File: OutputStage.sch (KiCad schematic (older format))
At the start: 6 parts, among them Q12 AO4468, Q13 AO4468, Q3 AO4468, Q5 AO4468, U5 LM5175PWPR

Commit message: Lots of changes for MFG: parts info
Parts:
- L2: SKU (none) -> MWSA0603S-2R2MT
- Q12, Q13, Q3, Q5: footprint (none) -> SmartBattery:SOIC-8_Alpha_Omega; SKU (none) -> AO4468
- U5: footprint IC_TPS61196PWPRQ1 -> SmartBattery:IC_TPS61196PWPRQ1; SKU (none) -> LM5175PWPR
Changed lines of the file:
@@
 F 0 "U5" H 3550 6220 50  0000 C CNN
 F 1 "LM5175PWPR" H 3550 6129 50  0000 C CNN
-F 2 "IC_TPS61196PWPRQ1" H 3550 4350 50  0001 L BNN
+F 2 "SmartBattery:IC_TPS61196PWPRQ1" H 3550 4350 50  0001 L BNN
 F 3 "" H 3550 4350 50  0001 L BNN
+F 4 "LM5175PWPR" H 3550 4350 50  0001 C CNN "SKU"
 	1    3550 4350
 	1    0    0    -1
@@
 F 0 "Q3" H 6106 2046 50  0000 L CNN
 F 1 "AO4468" H 6106 1955 50  0000 L CNN
-F 2 "" H 6100 2100 50  0001 C CNN
+F 2 "SmartBattery:SOIC-8_Alpha_Omega" H 6100 2100 50  0001 C CNN
 F 3 "~" H 5900 2000 50  0001 C CNN
+F 4 "AO4468" H 5900 2000 50  0001 C CNN "SKU"
 	1    5900 2000
 	1    0    0    -1
@@
 F 0 "Q12" H 7506 1996 50  0000 L CNN
 F 1 "AO4468" H 7506 1905 50  0000 L CNN
-F 2 "" H 7500 2050 50  0001 C CNN
+F 2 "SmartBattery:SOIC-8_Alpha_Omega" H 7500 2050 50  0001 C CNN
 F 3 "~" H 7300 1950 50  0001 C CNN
+F 4 "AO4468" H 7300 1950 50  0001 C CNN "SKU"
 	1    7300 1950
 	1    0    0    -1
@@
 F 0 "Q5" H 6106 2946 50  0000 L CNN
 F 1 "AO4468" H 6106 2855 50  0000 L CNN
-F 2 "" H 6100 3000 50  0001 C CNN
+F 2 "SmartBattery:SOIC-8_Alpha_Omega" H 6100 3000 50  0001 C CNN
 F 3 "~" H 5900 2900 50  0001 C CNN
+F 4 "AO4468" H 5900 2900 50  0001 C CNN "SKU"
 	1    5900 2900
 	1    0    0    -1
@@
 F 0 "Q13" H 7556 2996 50  0000 L CNN
 F 1 "AO4468" H 7556 2905 50  0000 L CNN
-F 2 "" H 7550 3050 50  0001 C CNN
+F 2 "SmartBattery:SOIC-8_Alpha_Omega" H 7550 3050 50  0001 C CNN
 F 3 "~" H 7350 2950 50  0001 C CNN
+F 4 "AO4468" H 7350 2950 50  0001 C CNN "SKU"
 	1    7350 2950
 	1    0    0    -1
@@
 F 2 "SmartBattery:MWSA0603" H 5900 3900 50  0001 C CNN
 F 3 "~" H 5900 3900 50  0001 C CNN
+F 4 "MWSA0603S-2R2MT" V 5900 3900 50  0001 C CNN "SKU"
 	1    5900 3900
 	0    1    1    0

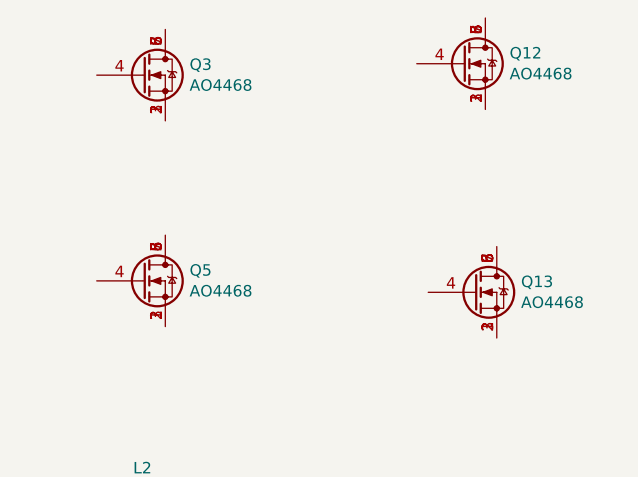
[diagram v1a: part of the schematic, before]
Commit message: Switching over to jlpcb
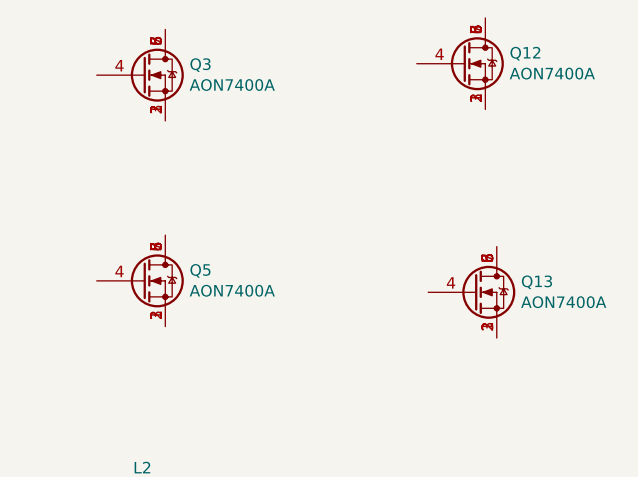
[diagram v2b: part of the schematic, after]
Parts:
- Q12, Q13, Q3, Q5: value AO4468 -> AON7400A; footprint SmartBattery:SOIC-8_Alpha_Omega -> lc_lib:QFN-8_3X3X065P; SKU AO4468 -> AON7400A
- U5: LCSC (none) -> C113356; SKU LM5175PWPR -> (none)
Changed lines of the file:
@@
 $Descr A4 11693 8268
 encoding utf-8
-Sheet 4 5
+Sheet 4 6
 Title ""
 Date ""
@@
 F 2 "SmartBattery:IC_TPS61196PWPRQ1" H 3550 4350 50  0001 L BNN
 F 3 "" H 3550 4350 50  0001 L BNN
-F 4 "LM5175PWPR" H 3550 4350 50  0001 C CNN "SKU"
+F 4 "C113356" H 3550 4350 50  0001 C CNN "LCSC"
 	1    3550 4350
 	1    0    0    -1
@@
 P 5900 2000
 F 0 "Q3" H 6106 2046 50  0000 L CNN
-F 1 "AO4468" H 6106 1955 50  0000 L CNN
-F 2 "SmartBattery:SOIC-8_Alpha_Omega" H 6100 2100 50  0001 C CNN
+F 1 "AON7400A " H 6106 1955 50  0000 L CNN
+F 2 "lc_lib:QFN-8_3X3X065P" H 6100 2100 50  0001 C CNN
 F 3 "~" H 5900 2000 50  0001 C CNN
-F 4 "AO4468" H 5900 2000 50  0001 C CNN "SKU"
+F 4 "AON7400A " H 5900 2000 50  0001 C CNN "SKU"
 	1    5900 2000
 	1    0    0    -1
@@
 P 7300 1950
 F 0 "Q12" H 7506 1996 50  0000 L CNN
-F 1 "AO4468" H 7506 1905 50  0000 L CNN
-F 2 "SmartBattery:SOIC-8_Alpha_Omega" H 7500 2050 50  0001 C CNN
+F 1 "AON7400A " H 7506 1905 50  0000 L CNN
+F 2 "lc_lib:QFN-8_3X3X065P" H 7500 2050 50  0001 C CNN
 F 3 "~" H 7300 1950 50  0001 C CNN
-F 4 "AO4468" H 7300 1950 50  0001 C CNN "SKU"
+F 4 "AON7400A " H 7300 1950 50  0001 C CNN "SKU"
 	1    7300 1950
 	1    0    0    -1
@@
 P 5900 2900
 F 0 "Q5" H 6106 2946 50  0000 L CNN
-F 1 "AO4468" H 6106 2855 50  0000 L CNN
-F 2 "SmartBattery:SOIC-8_Alpha_Omega" H 6100 3000 50  0001 C CNN
+F 1 "AON7400A " H 6106 2855 50  0000 L CNN
+F 2 "lc_lib:QFN-8_3X3X065P" H 6100 3000 50  0001 C CNN
 F 3 "~" H 5900 2900 50  0001 C CNN
-F 4 "AO4468" H 5900 2900 50  0001 C CNN "SKU"
+F 4 "AON7400A " H 5900 2900 50  0001 C CNN "SKU"
 	1    5900 2900
 	1    0    0    -1
@@
 P 7350 2950
 F 0 "Q13" H 7556 2996 50  0000 L CNN
-F 1 "AO4468" H 7556 2905 50  0000 L CNN
-F 2 "SmartBattery:SOIC-8_Alpha_Omega" H 7550 3050 50  0001 C CNN
+F 1 "AON7400A " H 7556 2905 50  0000 L CNN
+F 2 "lc_lib:QFN-8_3X3X065P" H 7550 3050 50  0001 C CNN
 F 3 "~" H 7350 2950 50  0001 C CNN
-F 4 "AO4468" H 7350 2950 50  0001 C CNN "SKU"
+F 4 "AON7400A " H 7350 2950 50  0001 C CNN "SKU"
 	1    7350 2950
 	1    0    0    -1

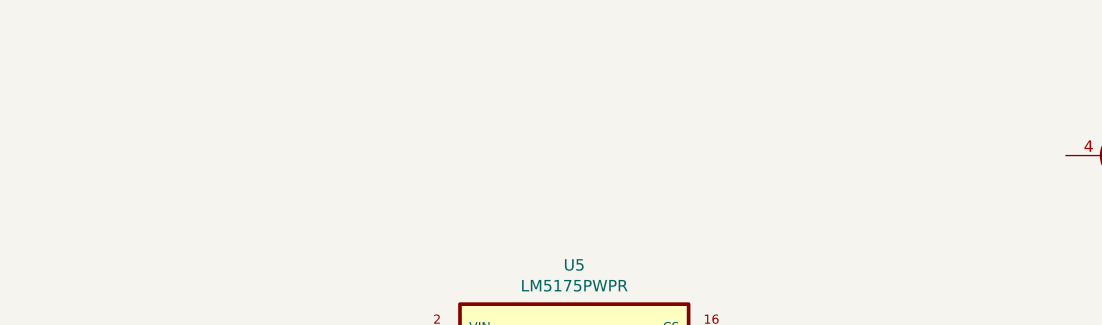
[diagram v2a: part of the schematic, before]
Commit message: Replaced old charger to support JLC assembly. Very close now!
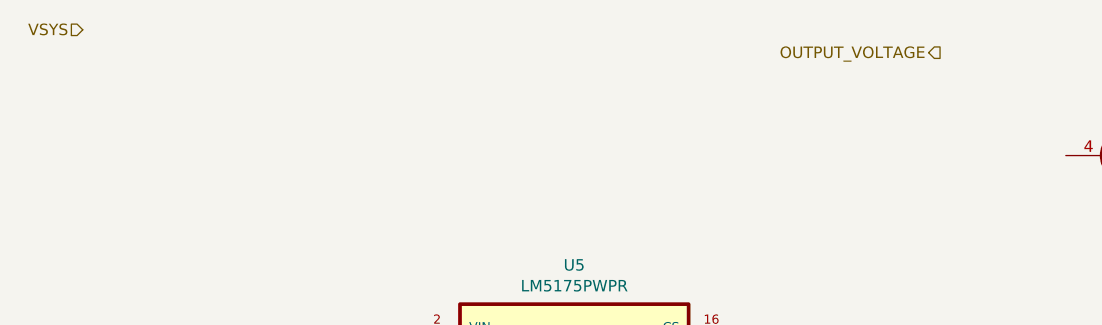
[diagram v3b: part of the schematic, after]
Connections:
- net labels added: OUTPUT_VOLTAGE, VSYS
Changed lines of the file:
@@
 Wire Wire Line
 	5200 3900 5750 3900
+Text HLabel 1400 1450 0    50   Input ~ 0
+VSYS
+Text HLabel 5150 1550 0    50   Output ~ 0
+OUTPUT_VOLTAGE
 $EndSCHEMATC

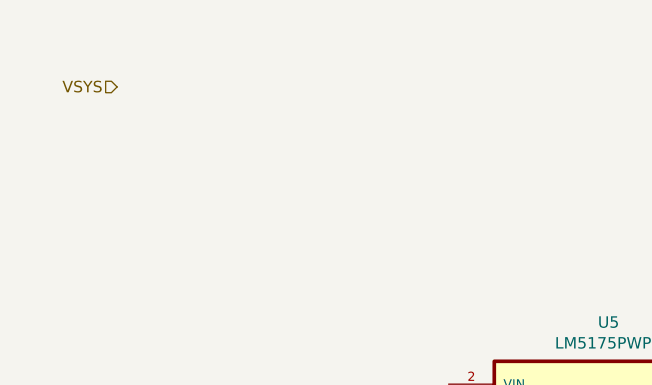
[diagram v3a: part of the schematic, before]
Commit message: Both type-c ports are done! Only outputstage left.
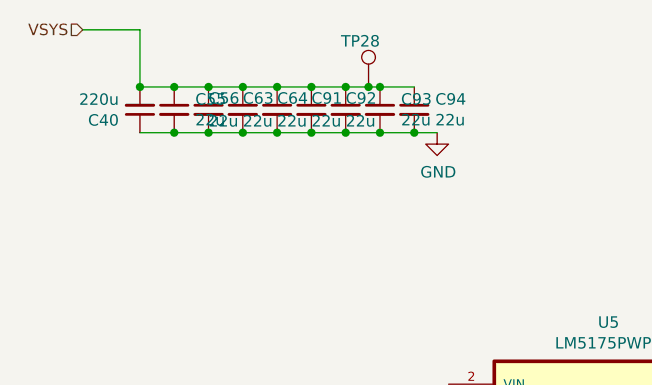
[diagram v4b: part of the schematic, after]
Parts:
- added C40: 220u, Capacitor_SMD:C_Elec_8x10.2, symbol Device:C_Small
- added C55, C56, C63, C64, C91, C92, C93, C94: 22u, lc_lib:0805_C, symbol Device:C_Small
- added TP28: TestPoint, TestPoint:TestPoint_Pad_D2.0mm, symbol Connector:TestPoint
- L2: footprint SmartBattery:MWSA0603 -> SmartBattery:L_10.3x11.5_H4
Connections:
- net labels added: GND
- wire segments 2 -> 22
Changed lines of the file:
@@
 $Descr A4 11693 8268
 encoding utf-8
-Sheet 4 6
+Sheet 4 8
 Title ""
 Date ""
@@
 F 0 "L2" V 5719 3900 50  0000 C CNN
 F 1 "MWSA0603-2R2MT" V 5810 3900 50  0000 C CNN
-F 2 "SmartBattery:MWSA0603" H 5900 3900 50  0001 C CNN
+F 2 "SmartBattery:L_10.3x11.5_H4" H 5900 3900 50  0001 C CNN
 F 3 "~" H 5900 3900 50  0001 C CNN
 F 4 "MWSA0603S-2R2MT" V 5900 3900 50  0001 C CNN "SKU"
@@
 Wire Wire Line
 	5200 3900 5750 3900
-Text HLabel 1400 1450 0    50   Input ~ 0
+Text HLabel 1250 1200 0    50   Input ~ 0
 VSYS
 Text HLabel 5150 1550 0    50   Output ~ 0
 OUTPUT_VOLTAGE
+$Comp
+L Device:C_Small C?
+U 1 1 5FF124CA
+P 1500 1550
+AR Path="/5FD99B08/5FF124CA" Ref="C?"  Part="1"
+AR Path="/60413DD6/5FF124CA" Ref="C40"  Part="1"
+F 0 "C40" H 1592 1596 50  0000 L CNN
+F 1 "220u" H 1592 1505 50  0000 L CNN
+F 2 "Capacitor_SMD:C_Elec_8x10.2" H 1500 1550 50  0001 C CNN
+F 3 "~" H 1500 1550 50  0001 C CNN
+F 4 "C311611" H 1500 1550 50  0001 C CNN "LCSC"
+	1    1500 1550
+	-1   0    0    1
+$EndComp
+$Comp
+L Connector:TestPoint TP?
+U 1 1 5FF124D0
+P 2500 1450
+AR Path="/5FD15753/5FF124D0" Ref="TP?"  Part="1"
+AR Path="/5FD99B08/5FF124D0" Ref="TP?"  Part="1"
+AR Path="/60413DD6/5FF124D0" Ref="TP28"  Part="1"
+F 0 "TP28" H 2550 1650 50  0000 R CNN
+F 1 "TestPoint" H 1950 1500 50  0001 R CNN
+F 2 "TestPoint:TestPoint_Pad_D2.0mm" H 2700 1450 50  0001 C CNN
+F 3 "~" H 2700 1450 50  0001 C CNN
+	1    2500 1450
+	1    0    0    -1
+$EndComp
+$Comp
+L Device:C_Small C?
+U 1 1 5FF12501
+P 2550 1550
+AR Path="/5FD99B08/5FF12501" Ref="C?"  Part="1"
+AR Path="/60413DD6/5FF12501" Ref="C93"  Part="1"
+F 0 "C93" H 2642 1596 50  0000 L CNN
+F 1 "22u" H 2642 1505 50  0000 L CNN
+F 2 "lc_lib:0805_C" H 2550 1550 50  0001 C CNN
+F 3 "~" H 2550 1550 50  0001 C CNN
+F 4 "C45783" H 2550 1550 50  0001 C CNN "LCSC"
+	1    2550 1550
+	1    0    0    -1
+$EndComp
+Connection ~ 2700 1650
+Wire Wire Line
+	2700 1650 2800 1650
+$Comp
+L power:GND #PWR0171
+U 1 1 5FF12523
+P 2800 1650
+F 0 "#PWR0171" H 2800 1400 50  0001 C CNN
+F 1 "GND" H 2805 1477 50  0000 C CNN
+F 2 "" H 2800 1650 50  0001 C CNN
+F 3 "" H 2800 1650 50  0001 C CNN
+	1    2800 1650
+	1    0    0    -1
+$EndComp
+Connection ~ 2500 1450
+Wire Wire Line
+	2500 1450 2550 1450
+Wire Wire Line
+	1500 1450 1650 1450
+Wire Wire Line
+	1800 1650 1950 1650
+$Comp
+L Device:C_Small C?
+U 1 1 5FF13851
+P 1800 1550
+AR Path="/5FD99B08/5FF13851" Ref="C?"  Part="1"
+AR Path="/60413DD6/5FF13851" Ref="C56"  Part="1"
+F 0 "C56" H 1800 1600 50  0000 L CNN
+F 1 "22u" H 1800 1500 50  0000 L CNN
+F 2 "lc_lib:0805_C" H 1800 1550 50  0001 C CNN
+F 3 "~" H 1800 1550 50  0001 C CNN
+F 4 "C45783" H 1800 1550 50  0001 C CNN "LCSC"
+	1    1800 1550
+	1    0    0    -1
+$EndComp
+Connection ~ 1800 1450
+Wire Wire Line
+	1800 1450 1950 1450
+$Comp
+L Device:C_Small C?
+U 1 1 5FF14635
+P 1950 1550
+AR Path="/5FD99B08/5FF14635" Ref="C?"  Part="1"
+AR Path="/60413DD6/5FF14635" Ref="C63"  Part="1"
+F 0 "C63" H 1950 1600 50  0000 L CNN
+F 1 "22u" H 1950 1500 50  0000 L CNN
+F 2 "lc_lib:0805_C" H 1950 1550 50  0001 C CNN
+F 3 "~" H 1950 1550 50  0001 C CNN
+F 4 "C45783" H 1950 1550 50  0001 C CNN "LCSC"
+	1    1950 1550
+	1    0    0    -1
+$EndComp
+Connection ~ 1950 1450
+Wire Wire Line
+	1950 1450 2100 1450
+Connection ~ 1950 1650
+Wire Wire Line
+	1950 1650 2100 1650
+$Comp
+L Device:C_Small C?
+U 1 1 5FF148DA
+P 2100 1550
+AR Path="/5FD99B08/5FF148DA" Ref="C?"  Part="1"
+AR Path="/60413DD6/5FF148DA" Ref="C64"  Part="1"
+F 0 "C64" H 2100 1600 50  0000 L CNN
+F 1 "22u" H 2100 1500 50  0000 L CNN
+F 2 "lc_lib:0805_C" H 2100 1550 50  0001 C CNN
+F 3 "~" H 2100 1550 50  0001 C CNN
+F 4 "C45783" H 2100 1550 50  0001 C CNN "LCSC"
+	1    2100 1550
+	1    0    0    -1
+$EndComp
+Connection ~ 2100 1450
+Wire Wire Line
+	2100 1450 2250 1450
+Connection ~ 2100 1650
+Wire Wire Line
+	2100 1650 2250 1650
+$Comp
+L Device:C_Small C?
+U 1 1 5FF14BE5
+P 2250 1550
+AR Path="/5FD99B08/5FF14BE5" Ref="C?"  Part="1"
+AR Path="/60413DD6/5FF14BE5" Ref="C91"  Part="1"
+F 0 "C91" H 2250 1600 50  0000 L CNN
+F 1 "22u" H 2250 1500 50  0000 L CNN
+F 2 "lc_lib:0805_C" H 2250 1550 50  0001 C CNN
+F 3 "~" H 2250 1550 50  0001 C CNN
+F 4 "C45783" H 2250 1550 50  0001 C CNN "LCSC"
+	1    2250 1550
+	1    0    0    -1
+$EndComp
+Connection ~ 2250 1450
+Wire Wire Line
+	2250 1450 2400 1450
+Connection ~ 2250 1650
+Wire Wire Line
+	2250 1650 2400 1650
+$Comp
+L Device:C_Small C?
+U 1 1 5FF14F44
+P 2400 1550
+AR Path="/5FD99B08/5FF14F44" Ref="C?"  Part="1"
+AR Path="/60413DD6/5FF14F44" Ref="C92"  Part="1"
+F 0 "C92" H 2400 1600 50  0000 L CNN
+F 1 "22u" H 2400 1500 50  0000 L CNN
+F 2 "lc_lib:0805_C" H 2400 1550 50  0001 C CNN
+F 3 "~" H 2400 1550 50  0001 C CNN
+F 4 "C45783" H 2400 1550 50  0001 C CNN "LCSC"
+	1    2400 1550
+	1    0    0    -1
+$EndComp
+Connection ~ 2400 1450
+Wire Wire Line
+	2400 1450 2500 1450
+Connection ~ 2400 1650
+Wire Wire Line
+	2400 1650 2550 1650
+Connection ~ 2550 1450
+Wire Wire Line
+	2550 1450 2700 1450
+Connection ~ 2550 1650
+Wire Wire Line
+	2550 1650 2700 1650
+$Comp
+L Device:C_Small C?
+U 1 1 5FF15579
+P 2700 1550
+AR Path="/5FD99B08/5FF15579" Ref="C?"  Part="1"
+AR Path="/60413DD6/5FF15579" Ref="C94"  Part="1"
+F 0 "C94" H 2792 1596 50  0000 L CNN
+F 1 "22u" H 2792 1505 50  0000 L CNN
+F 2 "lc_lib:0805_C" H 2700 1550 50  0001 C CNN
+F 3 "~" H 2700 1550 50  0001 C CNN
+F 4 "C45783" H 2700 1550 50  0001 C CNN "LCSC"
+	1    2700 1550
+	1    0    0    -1
+$EndComp
+$Comp
+L Device:C_Small C?
+U 1 1 5FF1591C
+P 1650 1550
+AR Path="/5FD99B08/5FF1591C" Ref="C?"  Part="1"
+AR Path="/60413DD6/5FF1591C" Ref="C55"  Part="1"
+F 0 "C55" H 1742 1596 50  0000 L CNN
+F 1 "22u" H 1742 1505 50  0000 L CNN
+F 2 "lc_lib:0805_C" H 1650 1550 50  0001 C CNN
+F 3 "~" H 1650 1550 50  0001 C CNN
+F 4 "C45783" H 1650 1550 50  0001 C CNN "LCSC"
+	1    1650 1550
+	1    0    0    -1
+$EndComp
+Connection ~ 1650 1450
+Wire Wire Line
+	1650 1450 1800 1450
+Wire Wire Line
+	1800 1650 1650 1650
+Connection ~ 1800 1650
+Wire Wire Line
+	1650 1650 1500 1650
+Connection ~ 1650 1650
+Wire Wire Line
+	1250 1200 1500 1200
+Wire Wire Line
+	1500 1200 1500 1450
+Connection ~ 1500 1450
 $EndSCHEMATC

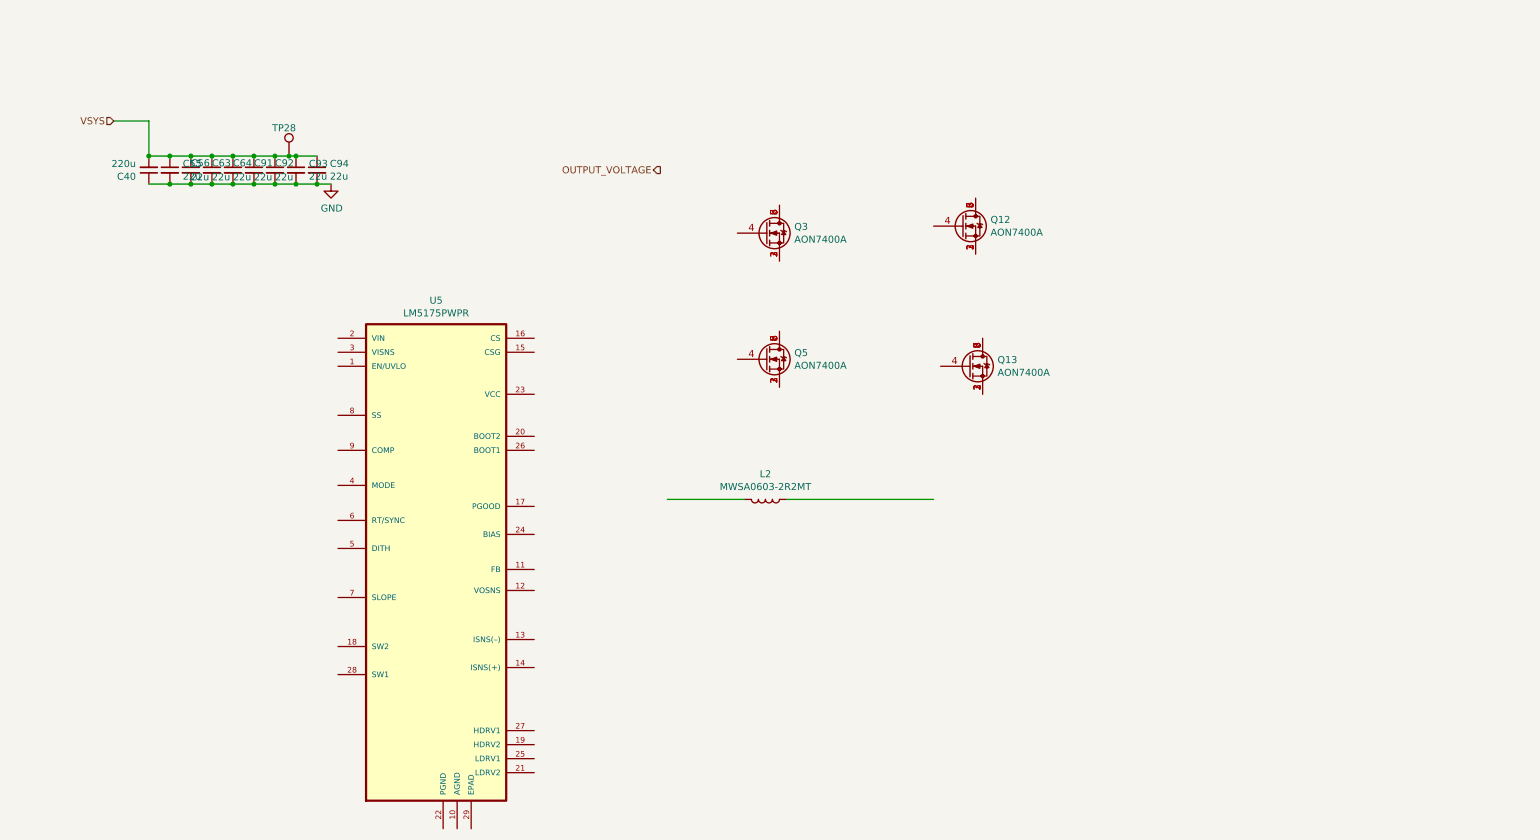
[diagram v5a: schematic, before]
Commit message: Type_A_implemented. Sch "locked". PCB Layout started.
*Changelog:
*Type-a switching regulator (TBD -- need to check inductor,caps, stability. Maybe check both peripherial inductors?)
*Type-A load switch + connector + esd
*started layout..
*found out that my footprint for n fet is wrong. Fixing now, need to replace all of those.
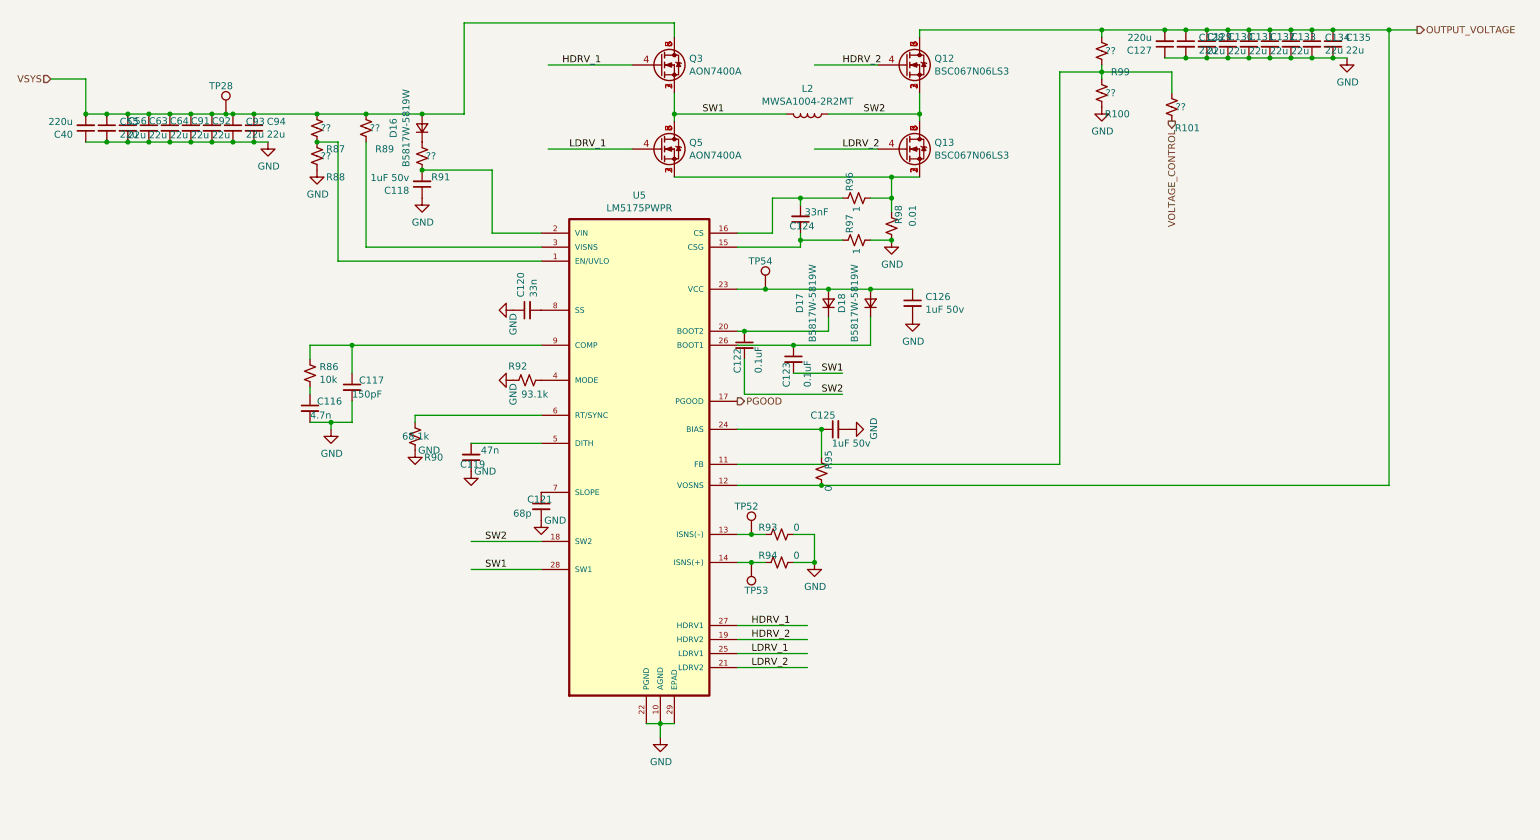
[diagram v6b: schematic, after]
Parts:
- added C116: 4.7n, lc_lib:0603_C, symbol Device:C_Small
- added C117: 150pF, lc_lib:0402_C, symbol Device:C_Small
- added C118, C125, C126: 1uF 50v, lc_lib:0402_C, symbol Device:C_Small
- added C119: 47n, lc_lib:0402_C, symbol Device:C_Small
- added C120: 33n, lc_lib:0402_C, symbol Device:C_Small
- added C121: 68p, lc_lib:0402_C, symbol Device:C_Small
- added C122, C123: 0.1uF, lc_lib:0402_C, symbol Device:C_Small
- added C124: 33nF, lc_lib:0402_C, symbol Device:C_Small
- added C127: 220u, Capacitor_SMD:C_Elec_8x10.2, symbol Device:C_Small
- added C128, C129, C130, C131, C132, C133, C134, C135: 22u, lc_lib:0805_C, symbol Device:C_Small
- added D16, D17, D18: B5817W-5819W, lc_lib:SOD-123, symbol Device:D_Small
- added R100, R101, R87, R88, R89, R91, R99: ??, lc_lib:0402_R, symbol Device:R_Small_US
- added R86: 10k, lc_lib:0402_R, symbol Device:R_Small_US
- added R90: 68.1k, lc_lib:0402_R, symbol Device:R_Small_US
- added R92: 93.1k, lc_lib:0402_R, symbol Device:R_Small_US
- added R93, R94, R95: 0, lc_lib:0402_R, symbol Device:R_Small_US
- added R96, R97: 1, lc_lib:0402_R, symbol Device:R_Small_US
- added R98: 0.01, lc_lib:2512_R, symbol Device:R_Small_US
- added TP52, TP53, TP54: TestPoint, TestPoint:TestPoint_Pad_D2.0mm, symbol Connector:TestPoint
- L2: value MWSA0603-2R2MT -> MWSA1004-2R2MT; LCSC (none) -> C149550; SKU MWSA0603S-2R2MT -> (none)
- Q12, Q13: value AON7400A -> BSC067N06LS3; footprint lc_lib:QFN-8_3X3X065P -> lc_lib:DFN-8_5X6MM; LCSC (none) -> C24199; SKU AON7400A -> (none)
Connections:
- net labels added: HDRV_1, HDRV_2, LDRV_1, LDRV_2, PGOOD, SW1, SW2, VOLTAGE_CONTROL
- wire segments 22 -> 136
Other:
- moved on the sheet: C40, C55, C56, C63, C64, C91, C92, C93, C94, Q3, Q5, TP28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
